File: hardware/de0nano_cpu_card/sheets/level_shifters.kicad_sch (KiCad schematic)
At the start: 36 parts, among them J2 EXP_HEADER_2x11, U1 SN74LVC8T245, U2 SN74LVC8T245, U3 SN74LVC8T245, U4 SN74LVC8T245, U5 SN74LVC8T245, U6 SN74LVC8T245, U8 SN74LVC8T245, U9 SN74LVC8T245

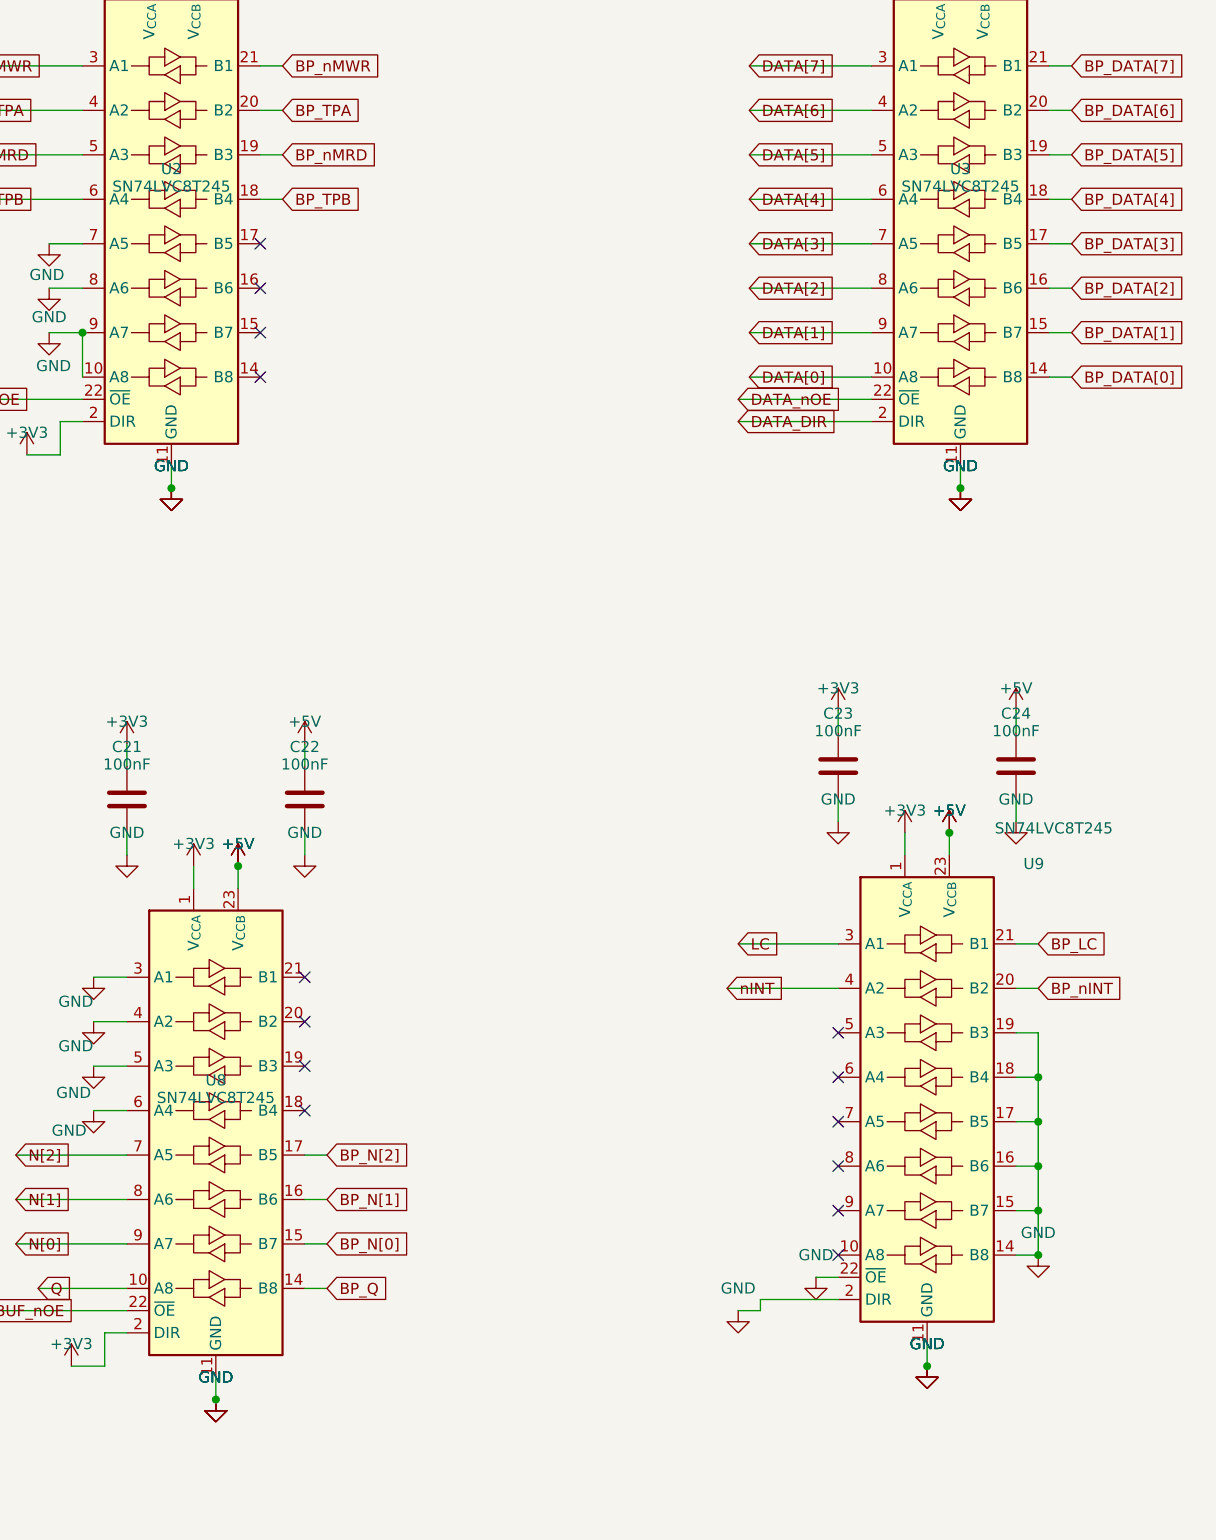
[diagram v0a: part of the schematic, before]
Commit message: Restore PWR_FLAGs, document 8-level-shifter GND-tie change
Schematic (user, GUI): re-added the 3 PWR_FLAG symbols (backplane +5V,
front-panel GND, Pico-W VSYS) that were deleted by mistake, clearing the
3 power_pin_not_driven ERC errors from the last round of edits. sch erc:
0 errors.

Docs: updated design_notes.md to match the user's own architecture
change made during final placement/routing -- level shifters increased
from 6 to 8 (U8/U9 added, both backplane-facing: 6 backplane + 2
future-expansion chips now), and all spare/unused channels across every
chip are now hard-tied to GND (no pull-up resistors), since DIR is
statically strapped on each chip (no bus-contention risk) and the
datasheet recommends tying off unused inputs. Updated BOM counts
accordingly (8x SN74LVC8T245, 16x decoupling caps, 25x pull-ups).
Status section and Next Steps rewritten to reflect that placement,
routing, and ground planes/via-stitching are done -- current phase is
Gerber export and JLCPCB handover.

Co-Authored-By: Claude Sonnet 5 <noreply@anthropic.com>
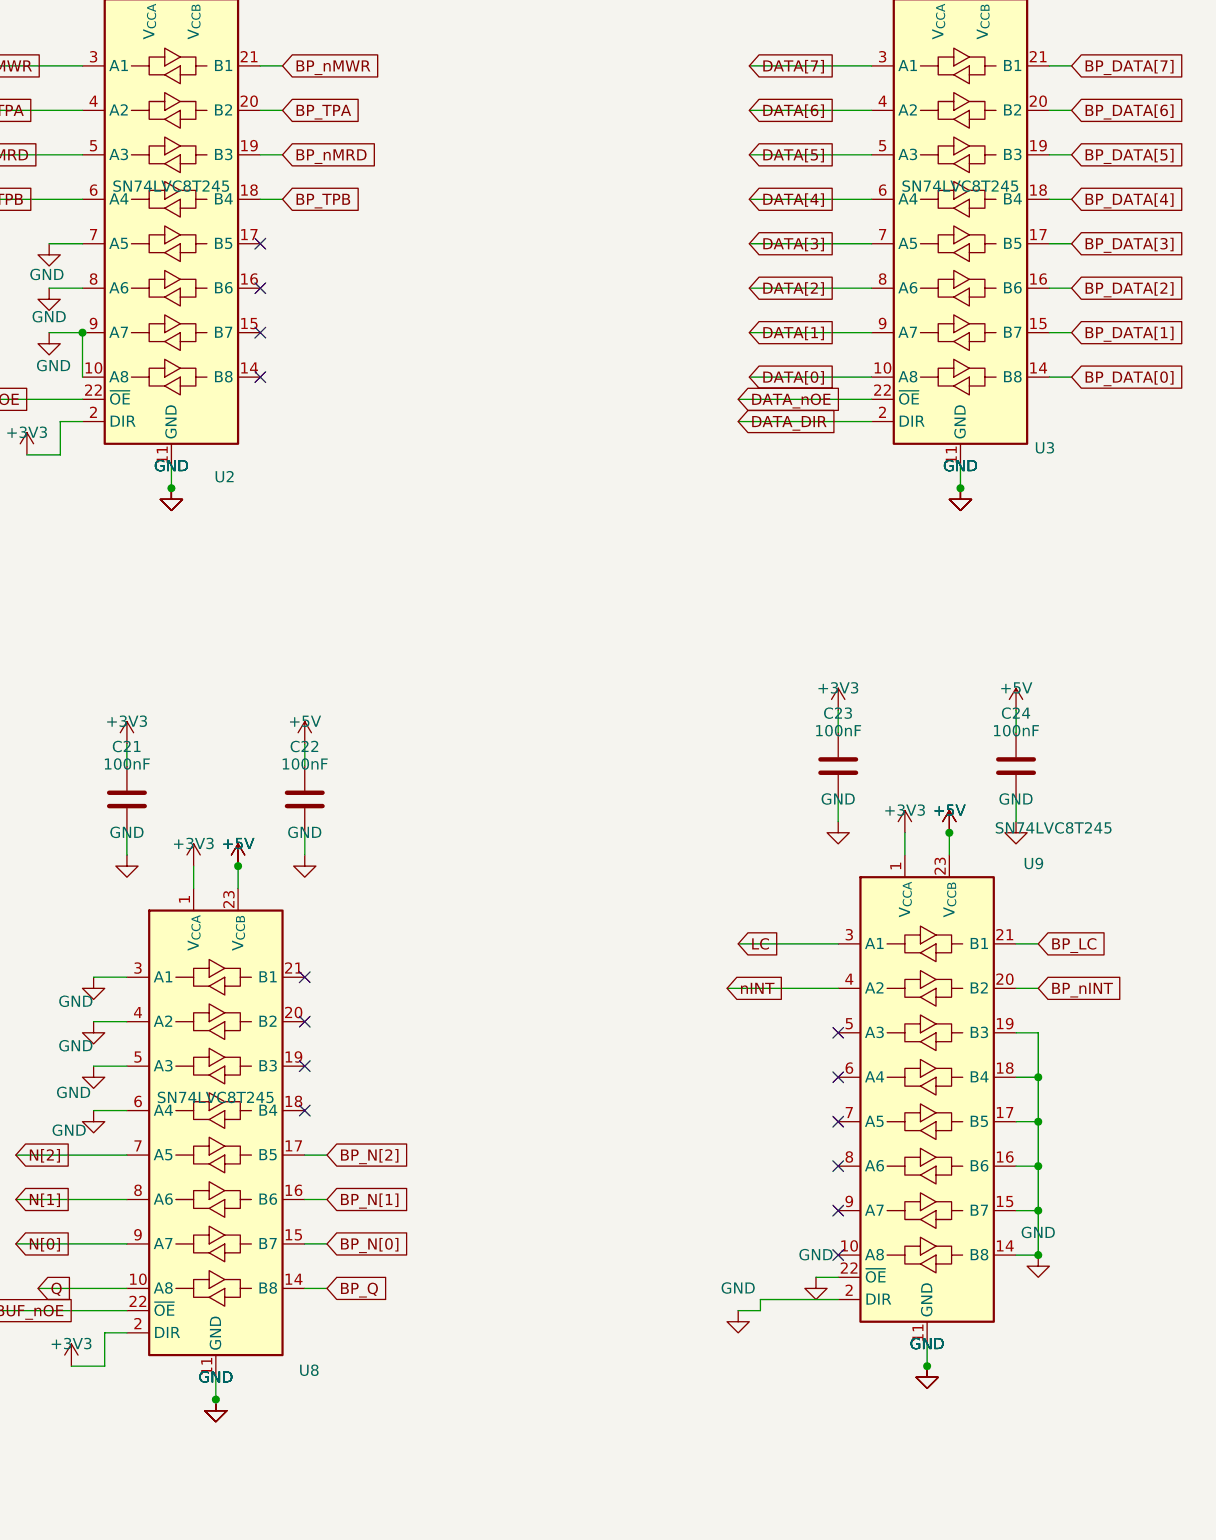
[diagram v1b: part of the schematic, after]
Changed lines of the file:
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@@
 		(dnp no)
 		(property "Reference" "U2"
-			(at 194.31 104.49 0)
+			(at 200.406 139.7 0)
 			(show_name no)
 			(do_not_autoplace no)
@@
 		(dnp no)
 		(property "Reference" "U3"
-			(at 284.48 104.49 0)
+			(at 294.132 136.398 0)
 			(show_name no)
 			(do_not_autoplace no)
@@
 		(dnp no)
 		(property "Reference" "U8"
-			(at 199.39 208.63 0)
+			(at 210.058 241.808 0)
 			(show_name no)
 			(do_not_autoplace no)
